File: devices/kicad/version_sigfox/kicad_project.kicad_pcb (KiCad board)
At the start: 2 copper layers, 8 parts, among them U1 SIM800L, U2 esp32_NodeMCU-track_chip, U3 GPS_PA6H, U4 bmp180-track_chip, U5 polulu, U7 charger_mr010

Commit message: [PCB] Premier jet Sigfox
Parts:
- removed C1: 100u, Capacitor_THT:CP_Axial_L10.0mm_D4.5mm_P15.00mm_Horizontal
- removed D1: 0.8V, Diode_THT:D_DO-15_P10.16mm_Horizontal
- removed U1: SIM800L, track_chip:SIM800L
- removed U5: polulu, track_chip:polulu
- added wisol1: brkws01, track_chip:BRWS01, F.Cu at (142.3, 94.5)
- moved U3 27.7 mm to (142.7, 84.5), turned to 90 degrees
- moved U7 25.5 mm to (122.7, 130.6), turned to 270 degrees
- moved U4 11.0 mm to (123.1, 64.8), turned to 180 degrees
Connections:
- U2 pad 1: Net-(U2-Pad1) -> (no net)
- U2 pad 10: Net-(U2-Pad10) -> (no net)
- U2 pad 11: Net-(U2-Pad11) -> (no net)
- U2 pad 12: Net-(U2-Pad12) -> (no net)
- U2 pad 13: Net-(U2-Pad13) -> (no net)
- U2 pad 14: Net-(U2-Pad14) -> (no net)
- U2 pad 18: Net-(U2-Pad18) -> (no net)
- U2 pad 19: Net-(U2-Pad19) -> RST_WSL
- U2 pad 2: Net-(U2-Pad2) -> (no net)
- U2 pad 23: Net-(U2-Pad23) -> (no net)
- U2 pad 24: Net-(U2-Pad24) -> (no net)
- U2 pad 25: Net-(U2-Pad25) -> (no net)
- U2 pad 27: RX0 -> (no net)
- U2 pad 3: Net-(U2-Pad3) -> (no net)
- U2 pad 30: Net-(U2-Pad30) -> (no net)
- U2 pad 4: Net-(U2-Pad4) -> (no net)
- U2 pad 5: Net-(U2-Pad5) -> (no net)
- U2 pad 6: Net-(U2-Pad6) -> (no net)
- U2 pad 7: Net-(U2-Pad7) -> (no net)
- U2 pad 8: Net-(U2-Pad8) -> (no net)
- U2 pad 9: Net-(U2-Pad9) -> (no net)
- U3 pad 1: Net-(U3-Pad1) -> (no net)
- U3 pad 3: Net-(U3-Pad3) -> (no net)
- U3 pad 4: Net-(U3-Pad4) -> (no net)
- U3 pad 6: RX0 -> (no net)
- U3 pad 9: Net-(U3-Pad9) -> (no net)
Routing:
- net EN_GPS: track 0.00 -> 111.5 mm
- net TX2: track 90.3 -> 13.7 mm
- net VBAT: track 107.4 -> 30.9 mm
- net RX2: track 88.1 -> 13.8 mm
- net 3.3V: track 0.00 -> 55.6 mm
- net RX0: track 37.5 -> 0.00 mm
- net Net-(C1-Pad1): track 23.6 -> 0.00 mm
- net Net-(D1-Pad2): track 18.5 -> 0.00 mm
- net SDA: track 33.3 -> 48.7 mm
- net 3V3: track 0.00 -> 13.6 mm
- net RST_WSL: track 0.00 -> 12.4 mm
- net TX0: track 37.4 -> 25.3 mm
- net GND: track 0.52 -> 0.00 mm

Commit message: [PCB] Ajout logo
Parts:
- added G***: LOGO, track_chip:logo, F.Cu at (150.2, 133.3)

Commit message: [PCB] Routage terminé + ajout logo
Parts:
- added U1: polulu, track_chip:polulu, F.Cu at (145.8, 128.2)
- moved G*** 15.3 mm to (165.5, 132.2), turned to 90 degrees
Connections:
- U2 pad 15: VBAT -> 5V
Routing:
- net 5V: track 0.00 -> 41.2 mm
- net EN_GPS: track 111.5 -> 97.5 mm
- net SDA: track 48.7 -> 59.7 mm
- net VBAT: track 30.9 -> 27.0 mm

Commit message: [PCB] Ajout du plan de coupe
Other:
- board outline added: 64.4 x 95.3 mm
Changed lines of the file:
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@@
   (general
     (thickness 1.6)
-    (drawings 0)
+    (drawings 4)
     (tracks 63)
     (zones 0)
@@
     (pad 20 thru_hole circle (at 0 -2.54) (size 1.524 1.524) (drill 0.762) (layers *.Cu *.Mask))
   )
+  (gr_line (start 102.108 144.4752) (end 166.5224 144.4244) (layer Edge.Cuts) (width 0.05))
+  (gr_line (start 102.108 49.1744) (end 166.4716 49.1744) (layer Edge.Cuts) (width 0.05))
+  (gr_line (start 166.4716 49.1744) (end 166.5224 144.4244) (layer Edge.Cuts) (width 0.05))
+  (gr_line (start 102.108 49.1744) (end 102.108 144.4752) (layer Edge.Cuts) (width 0.05))
   (segment (start 151.395199 83.069199) (end 151.395199 83.018399) (width 1) (layer B.Cu) (net 1))
   (segment (start 152.8572 84.5312) (end 151.395199 83.069199) (width 1) (layer B.Cu) (net 1))

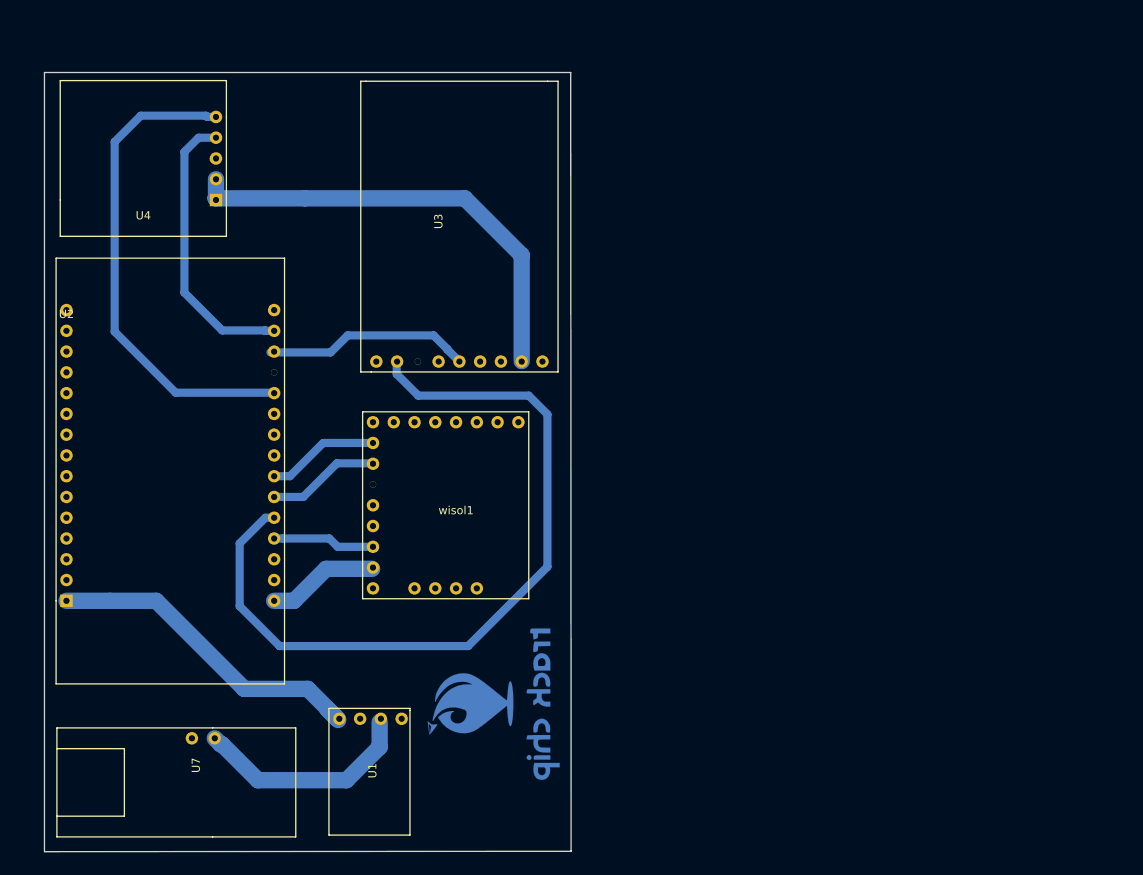
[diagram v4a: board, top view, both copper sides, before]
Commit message: [PCB] Ajout du plan de masse
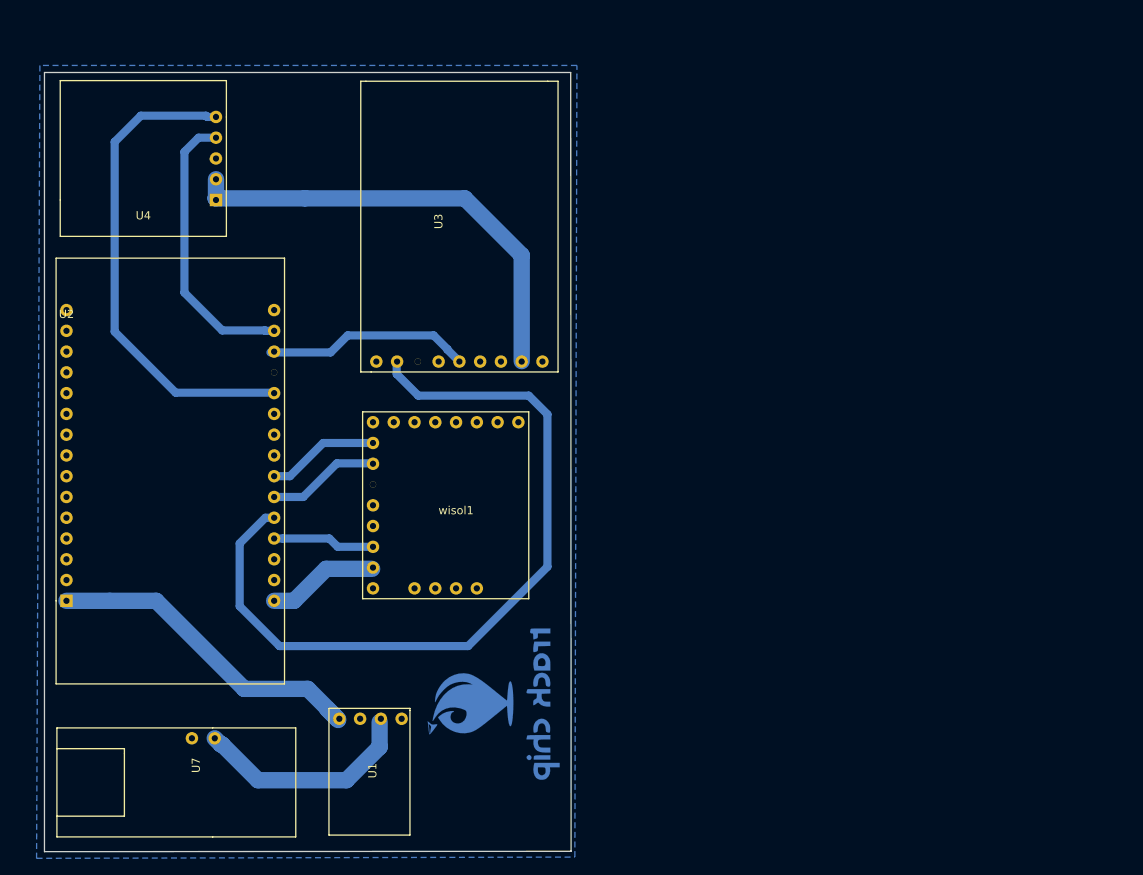
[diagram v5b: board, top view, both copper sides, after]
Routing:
- added copper zone on B.Cu, net GND
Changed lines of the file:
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@@
   (segment (start 126.5428 124.5616) (end 134.3152 124.5616) (width 2) (layer B.Cu) (net 12))
   (segment (start 134.3152 124.5616) (end 138.0236 128.27) (width 2) (layer B.Cu) (net 12))
+  (zone (net 2) (net_name GND) (layer B.Cu) (hatch edge 0.508)
+    (connect_pads (clearance 0.508))
+    (min_thickness 0.254)
+    (fill yes (arc_segments 32) (thermal_gap 0.508) (thermal_bridge_width 0.508))
+    (polygon
+      (pts
+        (xy 101.5492 48.3108) (xy 101.1428 145.288) (xy 166.9796 145.1356) (xy 167.2336 48.3108)
+      )
+    )
+  )
 )
